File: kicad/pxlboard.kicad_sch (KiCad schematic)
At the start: 37 parts, among them U1 XIAO-RP2040-SMD

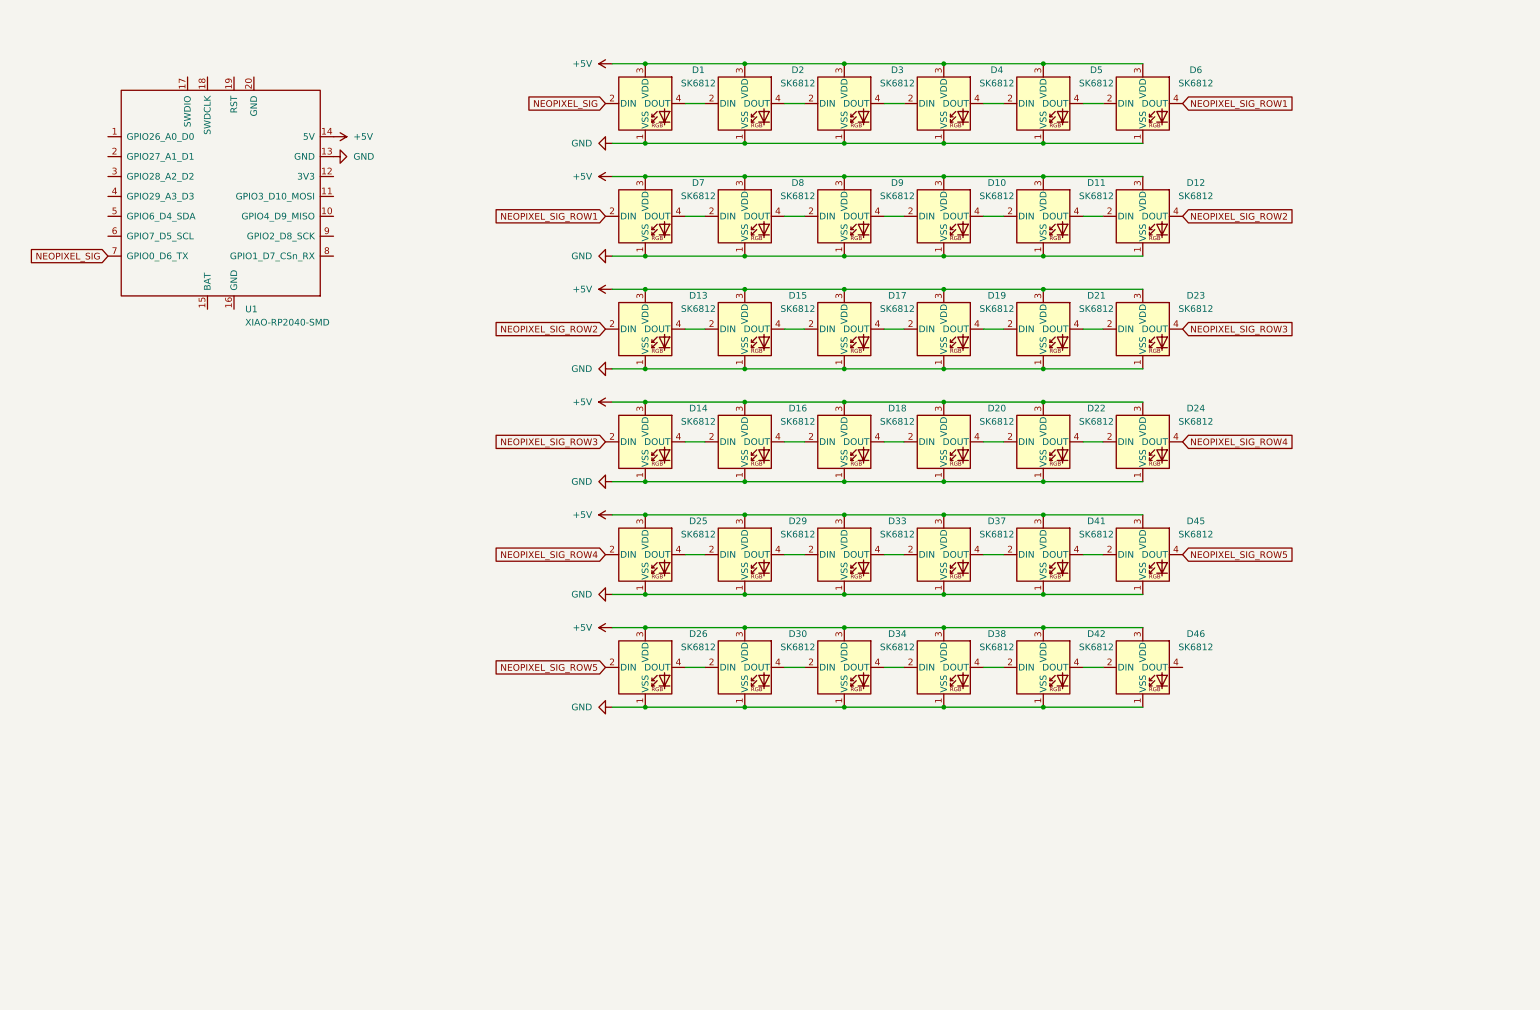
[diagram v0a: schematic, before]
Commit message: feat: add accelerometer
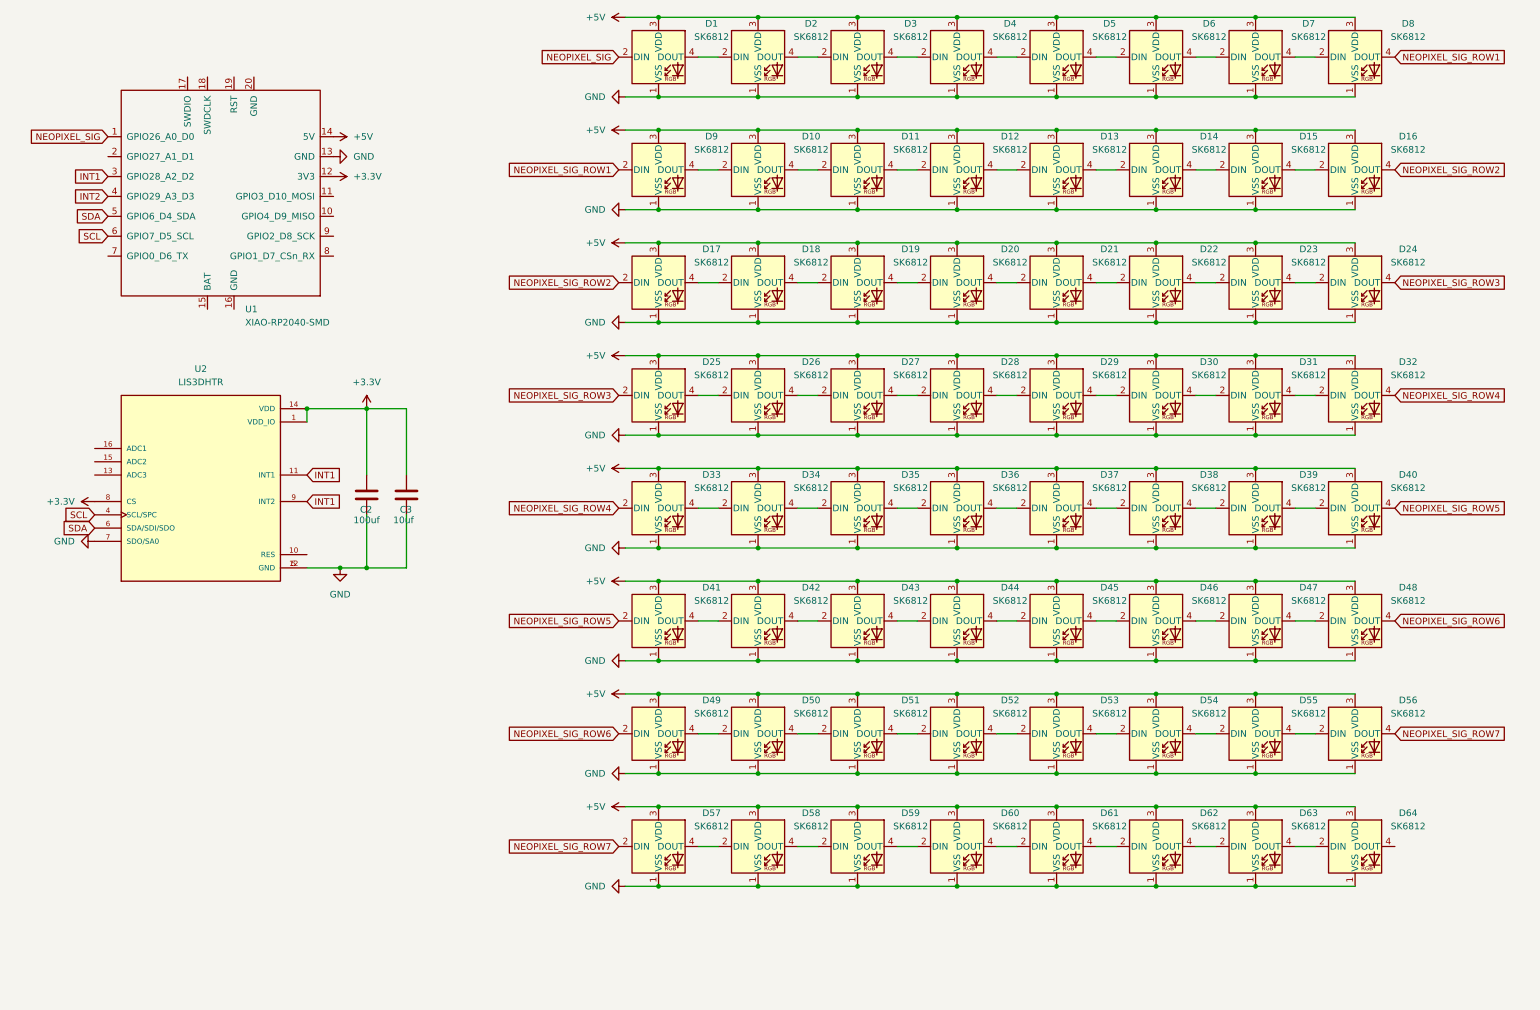
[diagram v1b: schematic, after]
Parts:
- added C2: 100uf, Capacitor_SMD:C_1206_3216Metric_Pad1.33x1.80mm_HandSolder, symbol Device:C
- added C3: 10uf, Capacitor_SMD:C_0402_1005Metric_Pad0.74x0.62mm_HandSolder, symbol Device:C
- added D27, D28, D31, D32, D35, D36, D39, D40, D43, D44, D47, D48, D49, D50, D51, D52, D53, D54, D55, D56, D57, D58, D59, D60, D61, D62, D63, D64: SK6812, LED_SMD:LED_SK6812_PLCC4_5.0x5.0mm_P3.2mm, symbol LED:SK6812
- added U2: LIS3DHTR, lib:XDCR_LIS3DHTR, symbol LIS3DHTR:LIS3DHTR
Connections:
- net +5V: now also D27.3 (VDD), D28.3 (VDD), D31.3 (VDD), D32.3 (VDD), D35.3 (VDD), D36.3 (VDD), D39.3 (VDD), D40.3 (VDD), D43.3 (VDD), D44.3 (VDD), D47.3 (VDD), D48.3 (VDD), D49.3 (VDD), D50.3 (VDD), D51.3 (VDD), D52.3 (VDD), D53.3 (VDD), D54.3 (VDD), D55.3 (VDD), D56.3 (VDD), D57.3 (VDD), D58.3 (VDD), D59.3 (VDD), D60.3 (VDD), D61.3 (VDD), D62.3 (VDD), D63.3 (VDD), D64.3 (VDD)
- net GND: now also C2.2, C3.2, D27.1 (VSS), D28.1 (VSS), D31.1 (VSS), D32.1 (VSS), D35.1 (VSS), D36.1 (VSS), D39.1 (VSS), D40.1 (VSS), D43.1 (VSS), D44.1 (VSS), D47.1 (VSS), D48.1 (VSS), D49.1 (VSS), D50.1 (VSS), D51.1 (VSS), D52.1 (VSS), D53.1 (VSS), D54.1 (VSS), D55.1 (VSS), D56.1 (VSS), D57.1 (VSS), D58.1 (VSS), D59.1 (VSS), D60.1 (VSS), D61.1 (VSS), D62.1 (VSS), D63.1 (VSS), D64.1 (VSS), U2.12 (GND), U2.5 (GND), U2.7 (SDO/SA0)
- net NEOPIXEL_SIG: now also U1.1 (GPIO26_A0_D0); no longer U1.7 (GPIO0_D6_TX)
- net NEOPIXEL_SIG_ROW1: now also D8.4 (DOUT), D9.2 (DIN); no longer D6.4 (DOUT), D7.2 (DIN)
- net NEOPIXEL_SIG_ROW2: now also D16.4 (DOUT), D17.2 (DIN); no longer D12.4 (DOUT), D13.2 (DIN)
- net NEOPIXEL_SIG_ROW3: now also D24.4 (DOUT), D25.2 (DIN); no longer D14.2 (DIN), D23.4 (DOUT)
- net NEOPIXEL_SIG_ROW4: now also D33.2 (DIN), D32.4 (DOUT); no longer D24.4 (DOUT), D25.2 (DIN)
- net NEOPIXEL_SIG_ROW5: now also D41.2 (DIN), D40.4 (DOUT); no longer D26.2 (DIN), D45.4 (DOUT)
- net +3.3V: now reaches U1.12 (3V3)
- net +3.3V: now also C2.1, C3.1, U2.1 (VDD_IO), U2.14 (VDD), U2.8 (CS)
- net INT1: now reaches U1.3 (GPIO28_A2_D2)
- net INT1: now also U2.11 (INT1), U2.9 (INT2)
- net INT2: now reaches U1.4 (GPIO29_A3_D3)
- net SDA: now reaches U1.5 (GPIO6_D4_SDA)
- net SDA: now also U2.6 (SDA/SDI/SDO)
- net SCL: now reaches U1.6 (GPIO7_D5_SCL)
- net SCL: now also U2.4 (SCL/SPC)
- net at D37.2 (DIN): now also D36.4 (DOUT); no longer D33.4 (DOUT)
- net at D37.4 (DOUT): now also D38.2 (DIN); no longer D41.2 (DIN)
- net at D15.2 (DIN): now also D14.4 (DOUT); no longer D13.4 (DOUT)
- net at D15.4 (DOUT): now also D16.2 (DIN); no longer D17.2 (DIN)
- net at D21.4 (DOUT): now also D22.2 (DIN); no longer D23.2 (DIN)
- net at D42.4 (DOUT): now also D43.2 (DIN); no longer D46.2 (DIN)
- net at D46.4 (DOUT): now also D47.2 (DIN)
- net at D19.2 (DIN): now also D18.4 (DOUT); no longer D17.4 (DOUT)
- net at D41.4 (DOUT): now also D42.2 (DIN); no longer D45.2 (DIN)
- net at D34.2 (DIN): now also D33.4 (DOUT); no longer D30.4 (DOUT)
- net at D34.4 (DOUT): now also D35.2 (DIN); no longer D38.2 (DIN)
- net at D26.4 (DOUT): now also D27.2 (DIN); no longer D30.2 (DIN)
- net at D18.2 (DIN): now also D17.4 (DOUT); no longer D16.4 (DOUT)
- net at D20.4 (DOUT): now also D21.2 (DIN); no longer D22.2 (DIN)
- net at D22.4 (DOUT): now also D23.2 (DIN); no longer D24.2 (DIN)
- net at D25.4 (DOUT): now also D26.2 (DIN); no longer D29.2 (DIN)
- net at D29.4 (DOUT): now also D30.2 (DIN); no longer D33.2 (DIN)
- net at D20.2 (DIN): now also D19.4 (DOUT); no longer D18.4 (DOUT)
- net at D38.4 (DOUT): now also D39.2 (DIN); no longer D42.2 (DIN)
- new net: D54.4 (DOUT), D55.2 (DIN)
- new net: D55.4 (DOUT), D56.2 (DIN)
- new net: D60.4 (DOUT), D61.2 (DIN)
- new net: D61.4 (DOUT), D62.2 (DIN)
- new net: D51.4 (DOUT), D52.2 (DIN)
- new net: D52.4 (DOUT), D53.2 (DIN)
- new net: D27.4 (DOUT), D28.2 (DIN)
- new net: D57.4 (DOUT), D58.2 (DIN)
- new net: D58.4 (DOUT), D59.2 (DIN)
- new net: D50.4 (DOUT), D51.2 (DIN)
- new net: D49.4 (DOUT), D50.2 (DIN)
- new net: D63.4 (DOUT), D64.2 (DIN)
- new net: D47.4 (DOUT), D48.2 (DIN)
- new net: D59.4 (DOUT), D60.2 (DIN)
- new net: D12.4 (DOUT), D13.2 (DIN)
- new net: D13.4 (DOUT), D14.2 (DIN)
- new net: D6.4 (DOUT), D7.2 (DIN)
- new net: D53.4 (DOUT), D54.2 (DIN)
- new net: D31.4 (DOUT), D32.2 (DIN)
- new net: D45.4 (DOUT), D46.2 (DIN)
- new net: D35.4 (DOUT), D36.2 (DIN)
- new net: D43.4 (DOUT), D44.2 (DIN)
- new net: D44.4 (DOUT), D45.2 (DIN)
- new net: D39.4 (DOUT), D40.2 (DIN)
- new net: D62.4 (DOUT), D63.2 (DIN)
- new net: D30.4 (DOUT), D31.2 (DIN)
- new net: D28.4 (DOUT), D29.2 (DIN)
- new net: D23.4 (DOUT), D24.2 (DIN)
- new net NEOPIXEL_SIG_ROW6: D48.4 (DOUT), D49.2 (DIN)
- new net NEOPIXEL_SIG_ROW7: D56.4 (DOUT), D57.2 (DIN)
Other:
- moved on the sheet: D1, D10, D11, D12, D13, D14, D15, D16, D18, D2, D20, D22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

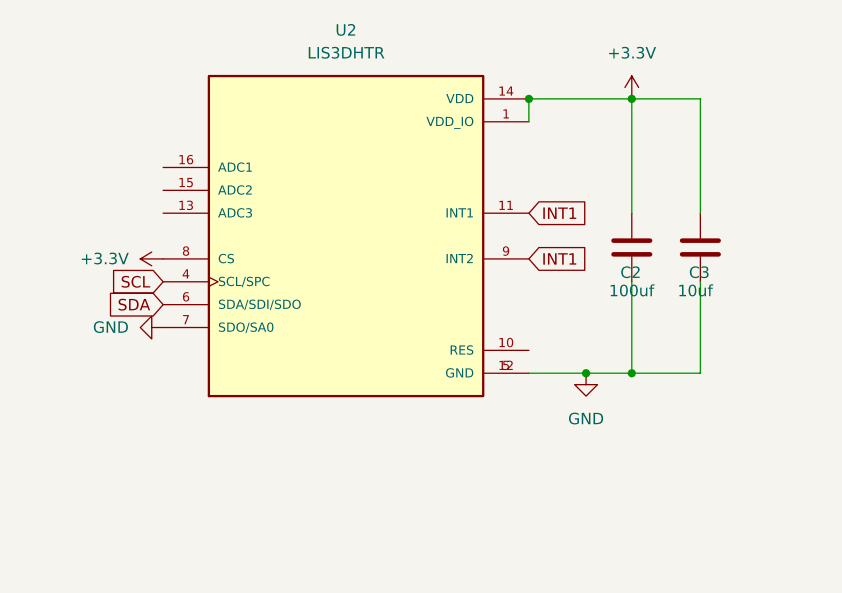
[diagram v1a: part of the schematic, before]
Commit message: feat: 64 leds and proper trace width
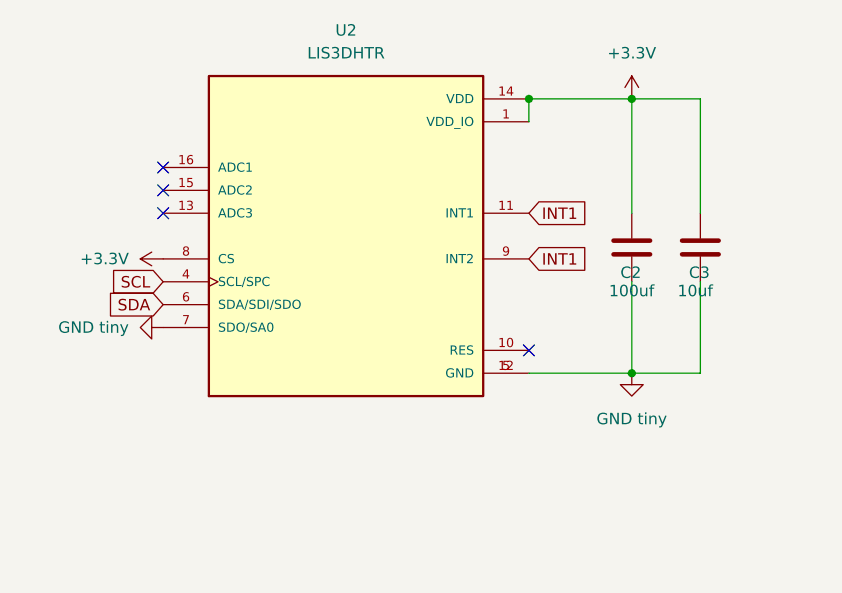
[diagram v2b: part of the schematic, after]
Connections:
- net GND: no longer C2.2, C3.2, U2.12 (GND), U2.5 (GND), U2.7 (SDO/SA0)
- new net GND tiny: C2.2, C3.2, U2.12 (GND), U2.5 (GND), U2.7 (SDO/SA0)
- no-connect marks 0 -> 4
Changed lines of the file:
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@@
 	)
 	(junction
-		(at 78.74 125.73)
-		(diameter 0)
-		(color 0 0 0 0)
-	)
-	(junction
 		(at 139.7 186.69)
 		(diameter 0)
@@
 		(color 0 0 0 0)
 	)
+	(no_connect
+		(at 72.39 123.19)
+	)
+	(no_connect
+		(at 31.75 105.41)
+	)
+	(no_connect
+		(at 31.75 102.87)
+	)
+	(no_connect
+		(at 31.75 107.95)
+	)
 	(wire
 		(pts
@@
 	(wire
 		(pts
-			(xy 78.74 125.73) (xy 83.82 125.73)
-		)
-		(stroke
-			(width 0)
-			(type default)
-		)
-	)
-	(wire
-		(pts
 			(xy 133.35 171.45) (xy 139.7 171.45)
 		)
@@
 	(wire
 		(pts
-			(xy 254 100.33) (xy 273.05 100.33)
+			(xy 72.39 125.73) (xy 83.82 125.73)
 		)
 		(stroke
@@
 	(wire
 		(pts
-			(xy 223.52 71.12) (xy 227.33 71.12)
+			(xy 254 100.33) (xy 273.05 100.33)
 		)
 		(stroke
@@
 	(wire
 		(pts
-			(xy 196.85 186.69) (xy 215.9 186.69)
+			(xy 223.52 71.12) (xy 227.33 71.12)
 		)
 		(stroke
@@
 	(wire
 		(pts
-			(xy 254 149.86) (xy 273.05 149.86)
+			(xy 196.85 186.69) (xy 215.9 186.69)
 		)
 		(stroke
@@
 	(wire
 		(pts
-			(xy 72.39 125.73) (xy 78.74 125.73)
+			(xy 254 149.86) (xy 273.05 149.86)
 		)
 		(stroke
@@
 	(symbol
 		(lib_id "power:GND")
+		(at 31.75 120.65 270)
+		(unit 1)
+		(exclude_from_sim no)
+		(in_bom yes)
+		(on_board yes)
+		(dnp no)
+		(fields_autoplaced yes)
+		(property "Reference" "#PWR019"
+			(at 25.4 120.65 0)
+			(effects
+				(hide yes)
+			)
+			(effects
+				(font
+					(size 1.27 1.27)
+				)
+			)
+		)
+		(property "Value" "GND tiny"
+			(at 27.94 120.6499 90)
+			(effects
+				(font
+					(size 1.27 1.27)
+				)
+				(justify right)
+			)
+		)
+		(property "Footprint" ""
+			(at 31.75 120.65 0)
+			(effects
+				(hide yes)
+			)
+			(effects
+				(font
+					(size 1.27 1.27)
+				)
+			)
+		)
+		(property "Datasheet" ""
+			(at 31.75 120.65 0)
+			(effects
+				(hide yes)
+			)
+			(effects
+				(font
+					(size 1.27 1.27)
+				)
+			)
+		)
+		(property "Description" "Power symbol creates a global label with name \"GND\" , ground"
+			(at 31.75 120.65 0)
+			(effects
+				(hide yes)
+			)
+			(effects
+				(font
+					(size 1.27 1.27)
+				)
+			)
+		)
+		(pin "1"
+		)
+		(instances
+			(project "pxlboard"
+				(path "/49fbc595-43cf-48e6-93ca-ce09759b59e5"
+					(reference "#PWR019")
+					(unit 1)
+				)
+			)
+		)
+	)
+	(symbol
+		(lib_id "power:GND")
 		(at 133.35 186.69 270)
 		(unit 1)
@@
 	)
 	(symbol
-		(lib_id "power:GND")
-		(at 78.74 125.73 0)
-		(unit 1)
-		(exclude_from_sim no)
-		(in_bom yes)
-		(on_board yes)
-		(dnp no)
-		(fields_autoplaced yes)
-		(property "Reference" "#PWR017"
-			(at 78.74 132.08 0)
-			(effects
-				(hide yes)
-			)
-			(effects
-				(font
-					(size 1.27 1.27)
-				)
-			)
-		)
-		(property "Value" "GND"
-			(at 78.74 130.81 0)
-			(effects
-				(font
-					(size 1.27 1.27)
-				)
-			)
-		)
-		(property "Footprint" ""
-			(at 78.74 125.73 0)
-			(effects
-				(hide yes)
-			)
-			(effects
-				(font
-					(size 1.27 1.27)
-				)
-			)
-		)
-		(property "Datasheet" ""
-			(at 78.74 125.73 0)
-			(effects
-				(hide yes)
-			)
-			(effects
-				(font
-					(size 1.27 1.27)
-				)
-			)
-		)
-		(property "Description" "Power symbol creates a global label with name \"GND\" , ground"
-			(at 78.74 125.73 0)
-			(effects
-				(hide yes)
-			)
-			(effects
-				(font
-					(size 1.27 1.27)
-				)
-			)
-		)
-		(pin "1"
-		)
-		(instances
-			(project "pxlboard"
-				(path "/49fbc595-43cf-48e6-93ca-ce09759b59e5"
-					(reference "#PWR017")
-					(unit 1)
-				)
-			)
-		)
-	)
-	(symbol
 		(lib_id "LED:SK6812")
 		(at 158.75 135.89 0)
@@
 	)
 	(symbol
+		(lib_id "power:GND")
+		(at 83.82 125.73 0)
+		(unit 1)
+		(exclude_from_sim no)
+		(in_bom yes)
+		(on_board yes)
+		(dnp no)
+		(fields_autoplaced yes)
+		(property "Reference" "#PWR017"
+			(at 83.82 132.08 0)
+			(effects
+				(hide yes)
+			)
+			(effects
+				(font
+					(size 1.27 1.27)
+				)
+			)
+		)
+		(property "Value" "GND tiny"
+			(at 83.82 130.81 0)
+			(effects
+				(font
+					(size 1.27 1.27)
+				)
+			)
+		)
+		(property "Footprint" ""
+			(at 83.82 125.73 0)
+			(effects
+				(hide yes)
+			)
+			(effects
+				(font
+					(size 1.27 1.27)
+				)
+			)
+		)
+		(property "Datasheet" ""
+			(at 83.82 125.73 0)
+			(effects
+				(hide yes)
+			)
+			(effects
+				(font
+					(size 1.27 1.27)
+				)
+			)
+		)
+		(property "Description" "Power symbol creates a global label with name \"GND\" , ground"
+			(at 83.82 125.73 0)
+			(effects
+				(hide yes)
+			)
+			(effects
+				(font
+					(size 1.27 1.27)
+				)
+			)
+		)
+		(pin "1"
+		)
+		(instances
+			(project "pxlboard"
+				(path "/49fbc595-43cf-48e6-93ca-ce09759b59e5"
+					(reference "#PWR017")
+					(unit 1)
+				)
+			)
+		)
+	)
+	(symbol
 		(lib_id "LIS3DHTR:LIS3DHTR")
 		(at 52.07 110.49 0)
@@
 		)
 		(instances
-			(project ""
+			(project "pxlboard"
 				(path "/49fbc595-43cf-48e6-93ca-ce09759b59e5"
 					(reference "#PWR01")
@@
 					(unit 1)
 				)
-			)
-		)
-	)
-	(symbol
-		(lib_id "power:GND")
-		(at 31.75 120.65 270)
-		(unit 1)
-		(exclude_from_sim no)
-		(in_bom yes)
-		(on_board yes)
-		(dnp no)
-		(fields_autoplaced yes)
-		(property "Reference" "#PWR019"
-			(at 25.4 120.65 0)
-			(effects
-				(hide yes)
-			)
-			(effects
-				(font
-					(size 1.27 1.27)
-				)
-			)
-		)
-		(property "Value" "GND"
-			(at 27.94 120.6499 90)
-			(effects
-				(font
-					(size 1.27 1.27)
-				)
-				(justify right)
-			)
-		)
-		(property "Footprint" ""
-			(at 31.75 120.65 0)
-			(effects
-				(hide yes)
-			)
-			(effects
-				(font
-					(size 1.27 1.27)
-				)
-			)
-		)
-		(property "Datasheet" ""
-			(at 31.75 120.65 0)
-			(effects
-				(hide yes)
-			)
-			(effects
-				(font
-					(size 1.27 1.27)
-				)
-			)
-		)
-		(property "Description" "Power symbol creates a global label with name \"GND\" , ground"
-			(at 31.75 120.65 0)
-			(effects
-				(hide yes)
-			)
-			(effects
-				(font
-					(size 1.27 1.27)
-				)
-			)
-		)
-		(pin "1"
-		)
-		(instances
-			(project "pxlboard"
-				(path "/49fbc595-43cf-48e6-93ca-ce09759b59e5"
-					(reference "#PWR019")
-					(unit 1)
-				)
